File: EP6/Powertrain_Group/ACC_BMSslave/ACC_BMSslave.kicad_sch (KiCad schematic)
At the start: 66 parts, among them IC1 ADBMS1818ASWAZ-R7, J1 B2B_CELL_TAPS_1, J10 isoSPI_out, J11 isoSPI_in, J2 B2B_NTC_1, J3 B2B_NTC_2, J4 B2B_CELL_TAPS_2, J5 B2B_NTC_3, J6 B2B_NTC_4, J7 GPIO, J8 RJ45, J9 RJ45, U1 LM324DT

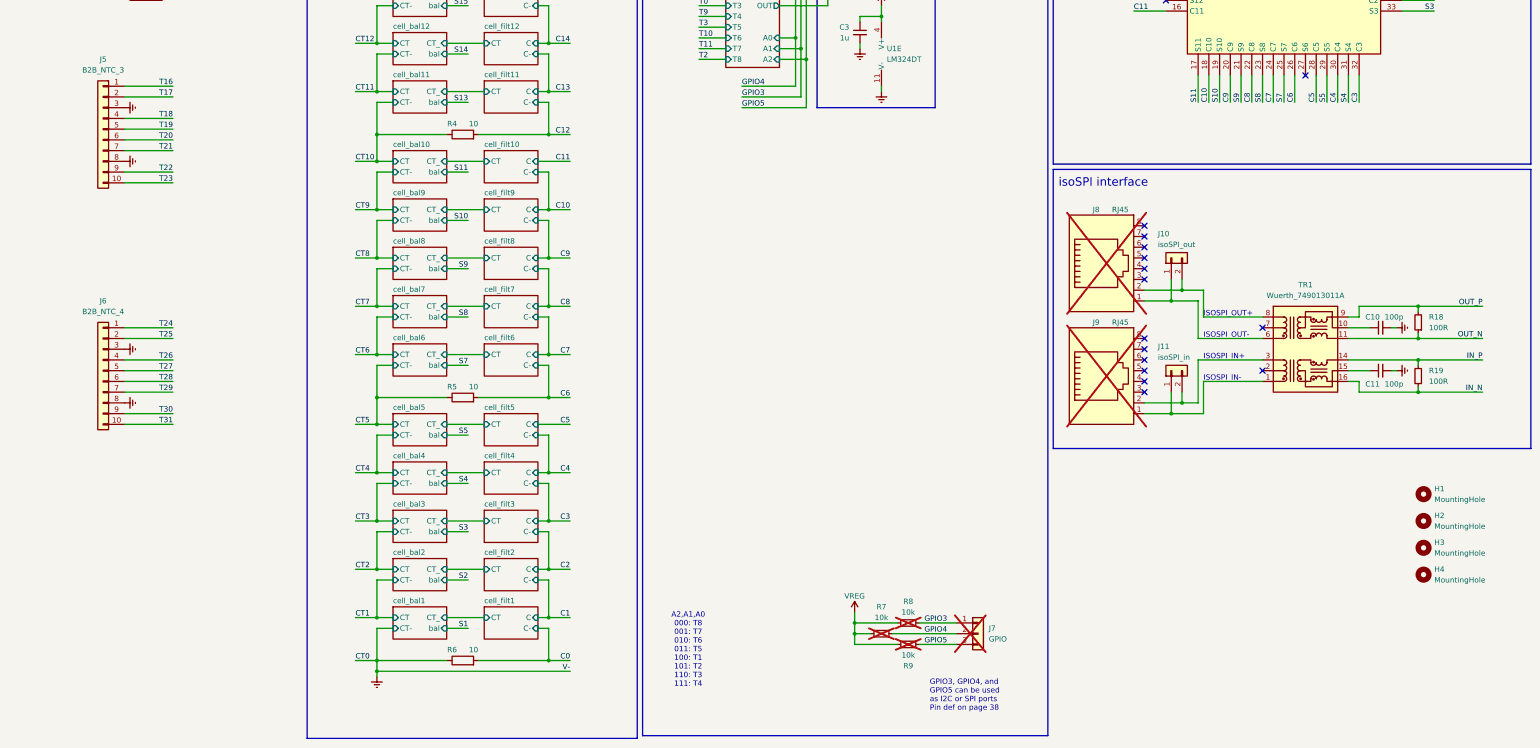
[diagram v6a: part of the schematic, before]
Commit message: [BMSslave] slave board done, connector board very not
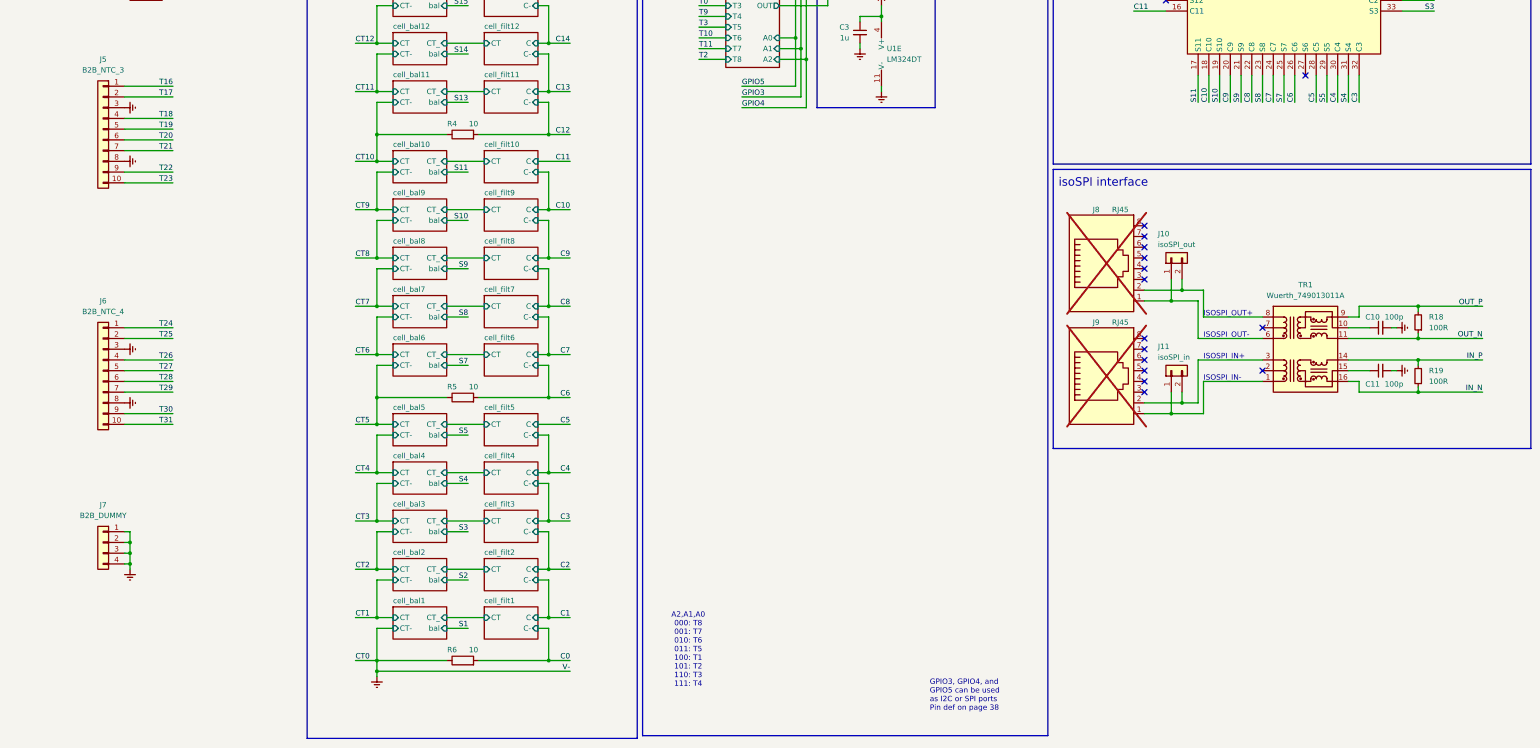
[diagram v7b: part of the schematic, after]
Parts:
- removed H1, H2, H3, H4: MountingHole, MountingHole:MountingHole_3.2mm_M3_DIN965, symbol Mechanical:MountingHole
- removed J7: GPIO, Connector_PinHeader_2.54mm:PinHeader_1x03_P2.54mm_Vertical, symbol Connector_Generic:Conn_01x03
- removed R7, R8, R9: 10k, Resistor_SMD:R_0402_1005Metric, symbol Device:R_Small
- added J7: B2B_DUMMY, Connector_PinHeader_2.54mm:PinHeader_1x04_P2.54mm_Vertical, symbol Connector_Generic:Conn_01x04
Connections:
- net Earth: now also J7.1 (Pin_1), J7.2 (Pin_2), J7.3 (Pin_3), J7.4 (Pin_4)

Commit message: [BMSslave] snapshot
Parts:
- removed J1: B2B_CELL_TAPS_1, Connector_PinHeader_2.54mm:PinHeader_1x16_P2.54mm_Vertical, symbol Connector_Generic:Conn_01x16
- removed J2: B2B_NTC_1, Connector_PinHeader_2.54mm:PinHeader_1x10_P2.54mm_Vertical, symbol Connector_Generic:Conn_01x10
- removed J3: B2B_NTC_2, Connector_PinHeader_2.54mm:PinHeader_1x10_P2.54mm_Vertical, symbol Connector_Generic:Conn_01x10
- removed J4: B2B_CELL_TAPS_2, Connector_PinHeader_2.54mm:PinHeader_1x16_P2.54mm_Vertical, symbol Connector_Generic:Conn_01x16
- removed J5: B2B_NTC_3, Connector_PinHeader_2.54mm:PinHeader_1x10_P2.54mm_Vertical, symbol Connector_Generic:Conn_01x10
- removed J6: B2B_NTC_4, Connector_PinHeader_2.54mm:PinHeader_1x10_P2.54mm_Vertical, symbol Connector_Generic:Conn_01x10
- removed J7: B2B_DUMMY, Connector_PinHeader_2.54mm:PinHeader_1x04_P2.54mm_Vertical, symbol Connector_Generic:Conn_01x04
- added H1, H2, H3, H4: MountingHole, MountingHole:MountingHole_4.3mm_M4_ISO14580, symbol Mechanical:MountingHole
- added J1, J2, J3, J4: JST XH, Connector_JST:JST_XH_B4B-XH-A_1x04_P2.50mm_Vertical, symbol Connector_Generic:Conn_01x04
- added J10, J11, J12, J13, J14, J15, J16, J17, J18, J19, J20, J21, J22, J23, J24, J25, J26, J27, J28, J29, J30, J31, J32, J33, J34, J35, J36, J5, J6, J7, J8, J9: JST ZH, Connector_JST:JST_ZH_B2B-ZR_1x02_P1.50mm_Vertical, symbol Connector_Generic:Conn_01x02
- renumbered J8 to J37, J9 to J38, J10 to J39, J11 to J40, R13 to R10, R14 to R11, R15 to R12, R16 to R13, R17 to R14, R18 to R15, R19 to R16, R10 to R7, R11 to R8, R12 to R9
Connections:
- net GPIO1: now also C4.1, R7.2
- net GPIO2: now also C5.1, R8.2
- net GPIO3: now also C7.1, R10.2
- net GPIO4: now also C6.1, R9.2
- net GPIO6: no longer C4.1, R7.2
- net GPIO7: no longer C5.1, R8.2
- net GPIO8: no longer C7.1, R10.2
- net GPIO9: no longer C6.1, R9.2
- net T0: now also J5.1 (Pin_1)
- net T1: now also J13.1 (Pin_1)
- net T10: now also J23.1 (Pin_1)
- net T11: now also J31.1 (Pin_1)
- net T12: now also J8.1 (Pin_1)
- net T13: now also J16.1 (Pin_1)
- net T14: now also J24.1 (Pin_1)
- net T15: now also J32.1 (Pin_1)
- net T16: now also J9.1 (Pin_1)
- net T17: now also J17.1 (Pin_1)
- net T18: now also J25.1 (Pin_1)
- net T19: now also J33.1 (Pin_1)
- net T2: now also J21.1 (Pin_1)
- net T20: now also J10.1 (Pin_1)
- net T21: now also J18.1 (Pin_1)
- net T22: now also J26.1 (Pin_1)
- net T23: now also J34.1 (Pin_1)
- net T24: now also J11.1 (Pin_1)
- net T25: now also J19.1 (Pin_1)
- net T26: now also J27.1 (Pin_1)
- net T27: now also J35.1 (Pin_1)
- net T28: now also J12.1 (Pin_1)
- net T29: now also J20.1 (Pin_1)
- net T3: now also J29.1 (Pin_1)
- net T30: now also J28.1 (Pin_1)
- net T31: now also J36.1 (Pin_1)
- net T4: now also J6.1 (Pin_1)
- net T5: now also J14.1 (Pin_1)
- net T6: now also J22.1 (Pin_1)
- net T7: now also J30.1 (Pin_1)
- net T8: now also J7.1 (Pin_1)
- net T9: now also J15.1 (Pin_1)
- net at F6.1: now also J2.2 (Pin_2)
- net at F10.1: now also J3.2 (Pin_2)
- net at F7.1: now also J2.3 (Pin_3)
- net at F5.1: now also J2.1 (Pin_1)
- net at F4.1: now also J1.4 (Pin_4)
- net at F1.1: now also J1.1 (Pin_1)
- net at F11.1: now also J3.3 (Pin_3)
- net at F12.1: now also J3.4 (Pin_4)
- net at F13.1: now also J4.1 (Pin_1)
- net at F14.1: now also J4.2 (Pin_2)
- net at F15.1: now also J4.3 (Pin_3)
- net at F16.1: now also J4.4 (Pin_4)
- net at F2.1: now also J1.2 (Pin_2)
- net at F3.1: now also J1.3 (Pin_3)
- net at F8.1: now also J2.4 (Pin_4)
- net at F9.1: now also J3.1 (Pin_1)
- new net GND: J10.2 (Pin_2), J11.2 (Pin_2), J12.2 (Pin_2), J13.2 (Pin_2), J14.2 (Pin_2), J15.2 (Pin_2), J16.2 (Pin_2), J17.2 (Pin_2), J18.2 (Pin_2), J19.2 (Pin_2), J20.2 (Pin_2), J21.2 (Pin_2), J22.2 (Pin_2), J23.2 (Pin_2), J24.2 (Pin_2), J25.2 (Pin_2), J26.2 (Pin_2), J27.2 (Pin_2), J28.2 (Pin_2), J29.2 (Pin_2), J30.2 (Pin_2), J31.2 (Pin_2), J32.2 (Pin_2), J33.2 (Pin_2), J34.2 (Pin_2), J35.2 (Pin_2), J36.2 (Pin_2), J5.2 (Pin_2), J6.2 (Pin_2), J7.2 (Pin_2), J8.2 (Pin_2), J9.2 (Pin_2)
